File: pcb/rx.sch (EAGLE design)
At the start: 34 parts, among them Y1 CRYSTAL-26MHZSMD-3.2X2.5

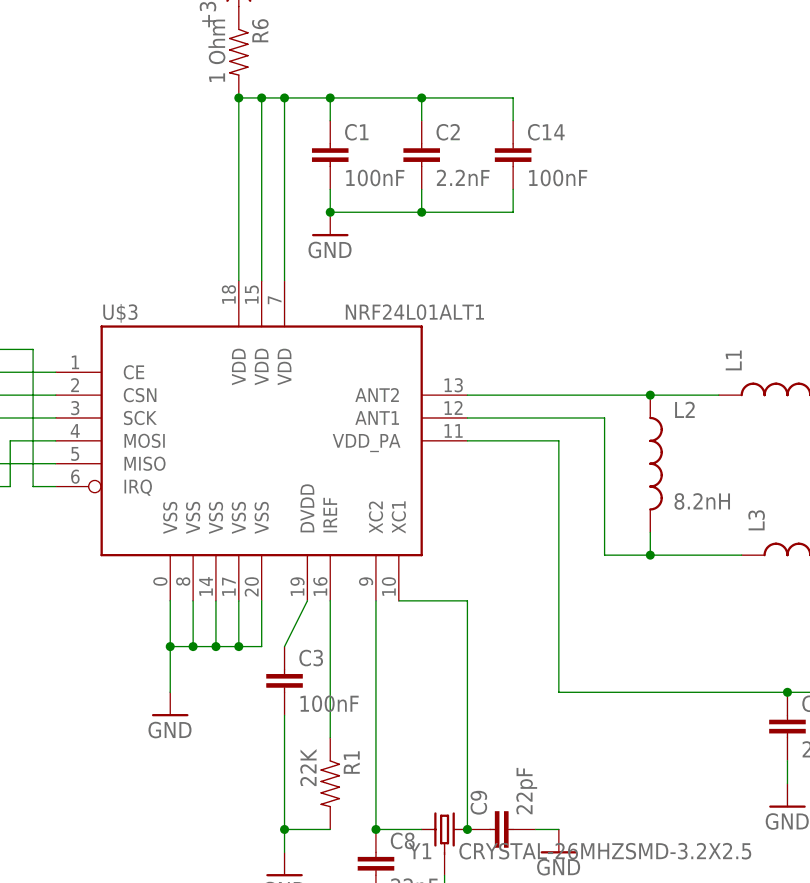
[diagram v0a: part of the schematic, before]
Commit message: adjusted RF section
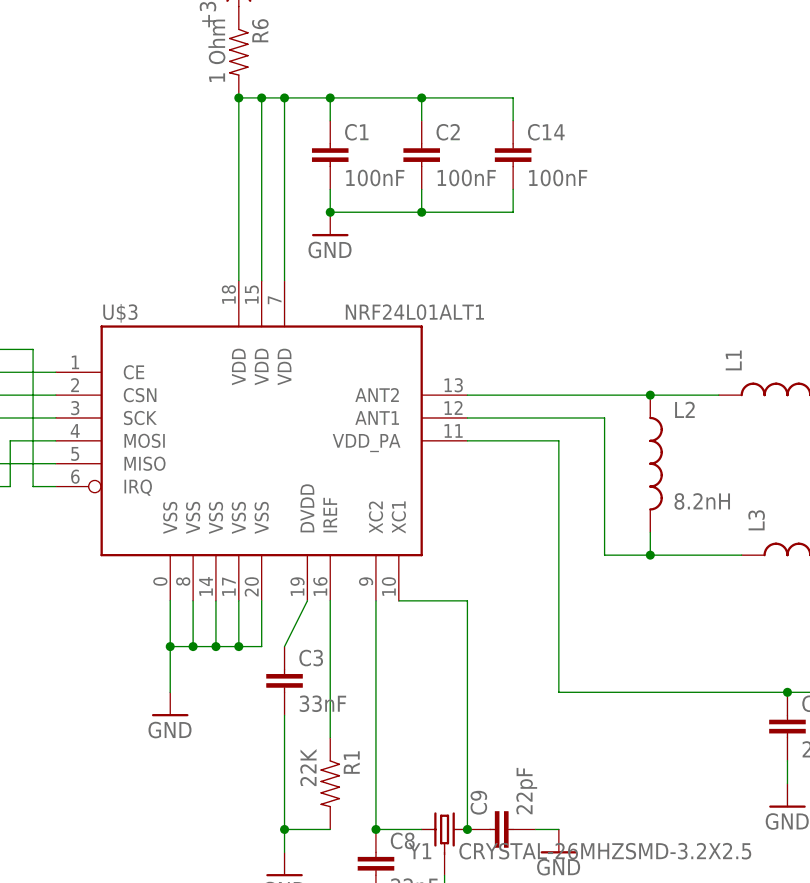
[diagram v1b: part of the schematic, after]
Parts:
- C2: value 2.2nF -> 100nF
- C3: value 100nF -> 33nF
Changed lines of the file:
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@@
 <part name="GND12" library="clock" deviceset="GND" device=""/>
 <part name="R1" library="joyAnalog" deviceset="RESISTOR" device="0805-RES" value="22K"/>
-<part name="C2" library="clock" deviceset="CAP" device="0805" value="2.2nF"/>
-<part name="C3" library="clock" deviceset="CAP" device="0805" value="100nF"/>
+<part name="C2" library="clock" deviceset="CAP" device="0805" value="100nF"/>
+<part name="C3" library="clock" deviceset="CAP" device="0805" value="33nF"/>
 <part name="GND2" library="clock" deviceset="GND" device=""/>
 <part name="L1" library="basicBoard" deviceset="INDUCTOR" device="0805" value="3.9nH"/>

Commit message: rev3 working
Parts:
- C1, C14, C2: value 100nF -> 4.7uF
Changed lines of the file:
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@@
 <part name="+3V1" library="supply1" library_urn="urn:adsk.eagle:library:371" deviceset="+3V3" device=""/>
 <part name="GND1" library="supply1" library_urn="urn:adsk.eagle:library:371" deviceset="GND" device=""/>
-<part name="C1" library="clock" deviceset="CAP" device="0805" value="100nF"/>
+<part name="C1" library="clock" deviceset="CAP" device="0805" value="4.7uF"/>
 <part name="GND12" library="clock" deviceset="GND" device=""/>
 <part name="R1" library="joyAnalog" deviceset="RESISTOR" device="0805-RES" value="22K"/>
-<part name="C2" library="clock" deviceset="CAP" device="0805" value="100nF"/>
+<part name="C2" library="clock" deviceset="CAP" device="0805" value="4.7uF"/>
 <part name="C3" library="clock" deviceset="CAP" device="0805" value="33nF"/>
 <part name="GND2" library="clock" deviceset="GND" device=""/>
@@
 <part name="GND13" library="supply1" library_urn="urn:adsk.eagle:library:371" deviceset="GND" device=""/>
 <part name="R6" library="joyAnalog" deviceset="RESISTOR" device="0805-RES" value="1 Ohm"/>
-<part name="C14" library="clock" deviceset="CAP" device="0805" value="100nF"/>
+<part name="C14" library="clock" deviceset="CAP" device="0805" value="4.7uF"/>
 </parts>
 <sheets>

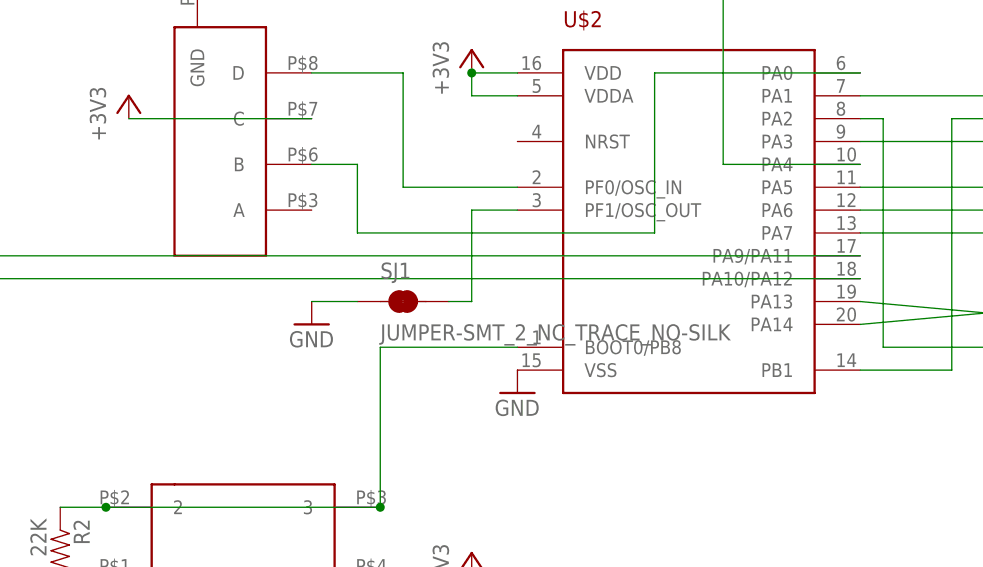
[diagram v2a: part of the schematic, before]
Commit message: tx board removed jumper
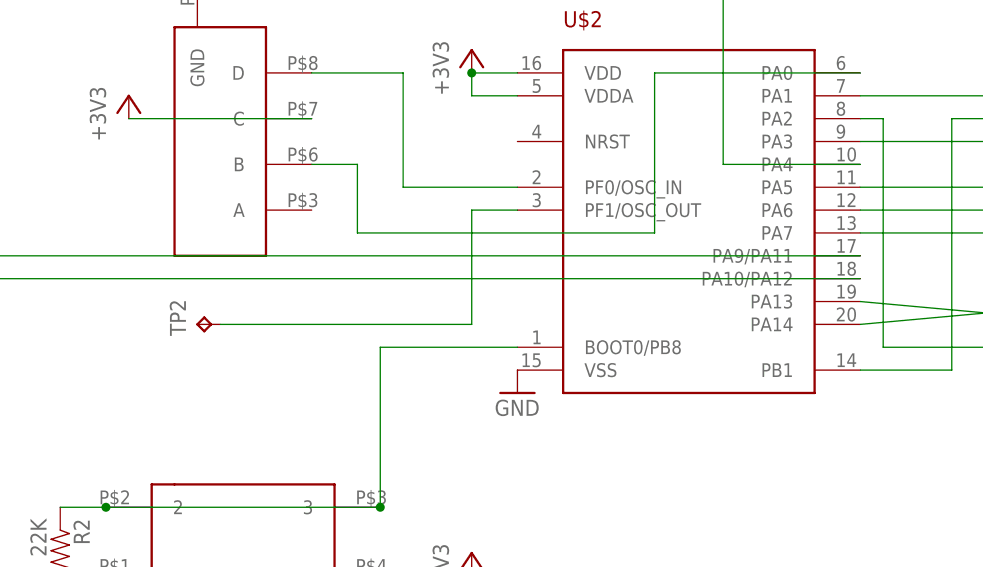
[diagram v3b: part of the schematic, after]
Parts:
- removed SJ1: JUMPER-SMT_2_NC_TRACE_NO-SILK, SparkFun-Jumpers:JUMPER-SMT_2_NC_TRACE_NO-SILK
- added TP2: TPTP12R, testpad:TPTP12R
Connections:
- net GND: no longer SJ1.1
- net N$19: now also TP2.TP; no longer SJ1.2
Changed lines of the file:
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@@
 <part name="R4" library="joyAnalog" deviceset="RESISTOR" device="0805-RES" value="5.1K"/>
 <part name="P+1" library="supply1" library_urn="urn:adsk.eagle:library:371" deviceset="+5V" device=""/>
-<part name="SJ1" library="SparkFun-Jumpers" deviceset="JUMPER-SMT_2_NC_TRACE" device="_NO-SILK"/>
 <part name="U$10" library="3pos_slide_switch" deviceset="324_SW" device="324_SWITCH_FOOT_HOLE" value="324_SW324_SWITCH_FOOT_HOLE"/>
 <part name="LED2" library="joyAnalog" deviceset="LED" device="CHIP-LED0805"/>
@@
 <part name="E1" library="SparkFun-RF" deviceset="ANTENNA-GROUNDED" device="TRACE-15.2MM"/>
 <part name="GND6" library="clock" deviceset="GND" device=""/>
-<part name="GND13" library="supply1" library_urn="urn:adsk.eagle:library:371" deviceset="GND" device=""/>
 <part name="R6" library="joyAnalog" deviceset="RESISTOR" device="0805-RES" value="1 Ohm"/>
 <part name="C14" library="clock" deviceset="CAP" device="0805" value="4.7uF"/>
+<part name="TP2" library="testpad" library_urn="urn:adsk.eagle:library:385" deviceset="TP" device="TP12R" package3d_urn="urn:adsk.eagle:package:27963/1"/>
 </parts>
 <sheets>
@@
 <instance part="R4" gate="G$1" x="30.48" y="43.18"/>
 <instance part="P+1" gate="1" x="-137.16" y="0"/>
-<instance part="SJ1" gate="G$1" x="0" y="0"/>
 <instance part="U$10" gate="G$1" x="-17.78" y="-27.94"/>
 <instance part="LED2" gate="G$1" x="17.78" y="43.18" rot="R270"/>
@@
 <instance part="E1" gate="G$1" x="241.3" y="17.78" rot="R270"/>
 <instance part="GND6" gate="1" x="231.14" y="7.62"/>
-<instance part="GND13" gate="1" x="-10.16" y="-2.54"/>
 <instance part="R6" gate="G$1" x="116.84" y="55.88" rot="R270"/>
 <instance part="C14" gate="G$1" x="147.32" y="43.18"/>
+<instance part="TP2" gate="G$1" x="-22.86" y="-2.54" rot="R90"/>
 </instances>
 <busses>
@@
 <pinref part="GND6" gate="1" pin="GND"/>
 <wire x1="231.14" y1="15.24" x2="231.14" y2="10.16" width="0.1524" layer="91"/>
-</segment>
-<segment>
-<pinref part="SJ1" gate="G$1" pin="1"/>
-<wire x1="-10.16" y1="0" x2="-5.08" y2="0" width="0.1524" layer="91"/>
-<pinref part="GND13" gate="1" pin="GND"/>
 </segment>
 </net>
@@
 <pinref part="U$2" gate="G$1" pin="PF1/OSC_OUT"/>
 <wire x1="12.7" y1="10.16" x2="7.62" y2="10.16" width="0.1524" layer="91"/>
-<wire x1="7.62" y1="10.16" x2="7.62" y2="0" width="0.1524" layer="91"/>
-<pinref part="SJ1" gate="G$1" pin="2"/>
-<wire x1="7.62" y1="0" x2="5.08" y2="0" width="0.1524" layer="91"/>
+<wire x1="7.62" y1="10.16" x2="7.62" y2="-2.54" width="0.1524" layer="91"/>
+<wire x1="7.62" y1="-2.54" x2="-20.32" y2="-2.54" width="0.1524" layer="91"/>
+<pinref part="TP2" gate="G$1" pin="TP"/>
 </segment>
 </net>
@@
 will not be understood (or retained) with this version.
 </note>
+<note version="8.3" severity="warning">
+Since Version 8.3, EAGLE supports the association of 3D packages
+with devices in libraries, schematics, and board files. Those 3D
+packages will not be understood (or retained) with this version.
+</note>
 </compatibility>

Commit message: before trail run
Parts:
- C3: value 33nF -> 100nF
- C8, C9: value 22pF -> 12pF
- Y1: value CRYSTAL-26MHZSMD-3.2X2.5 -> 16MHz_12pF
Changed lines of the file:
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@@
 <part name="R1" library="joyAnalog" deviceset="RESISTOR" device="0805-RES" value="22K"/>
 <part name="C2" library="clock" deviceset="CAP" device="0805" value="4.7uF"/>
-<part name="C3" library="clock" deviceset="CAP" device="0805" value="33nF"/>
+<part name="C3" library="clock" deviceset="CAP" device="0805" value="100nF"/>
 <part name="GND2" library="clock" deviceset="GND" device=""/>
 <part name="L1" library="basicBoard" deviceset="INDUCTOR" device="0805" value="3.9nH"/>
@@
 <part name="GND5" library="clock" deviceset="GND" device=""/>
 <part name="GND8" library="clock" deviceset="GND" device=""/>
-<part name="C8" library="clock" deviceset="CAP" device="0805" value="22pF"/>
+<part name="C8" library="clock" deviceset="CAP" device="0805" value="12pF"/>
 <part name="GND10" library="clock" deviceset="GND" device=""/>
-<part name="C9" library="clock" deviceset="CAP" device="0805" value="22pF"/>
+<part name="C9" library="clock" deviceset="CAP" device="0805" value="12pF"/>
 <part name="GND11" library="clock" deviceset="GND" device=""/>
 <part name="U$4" library="3pos_slide_switch" deviceset="XC6206_DEV" device=""/>
@@
 <part name="GND16" library="supply1" library_urn="urn:adsk.eagle:library:371" deviceset="GND" device=""/>
 <part name="GND17" library="supply1" library_urn="urn:adsk.eagle:library:371" deviceset="GND" device=""/>
-<part name="Y1" library="SparkFun-Clocks" deviceset="CRYSTAL-26MHZ" device="SMD-3.2X2.5"/>
+<part name="Y1" library="SparkFun-Clocks" deviceset="CRYSTAL-26MHZ" device="SMD-3.2X2.5" value="16MHz_12pF"/>
 <part name="R2" library="joyAnalog" deviceset="RESISTOR" device="0805-RES" value="22K"/>
 <part name="GND9" library="supply1" library_urn="urn:adsk.eagle:library:371" deviceset="GND" device=""/>
@@
 <instance part="GND10" gate="1" x="132.08" y="-45.72"/>
 <instance part="C9" gate="G$1" x="147.32" y="-30.48" rot="R90"/>
-<instance part="GND11" gate="1" x="152.4" y="-33.02"/>
+<instance part="GND11" gate="1" x="162.56" y="-33.02"/>
 <instance part="U$4" gate="G$1" x="-116.84" y="-7.62"/>
 <instance part="C10" gate="G$1" x="-137.16" y="-10.16"/>
@@
 <pinref part="C9" gate="G$1" pin="2"/>
 <pinref part="GND11" gate="1" pin="GND"/>
-<wire x1="152.4" y1="-30.48" x2="149.86" y2="-30.48" width="0.1524" layer="91"/>
+<wire x1="162.56" y1="-30.48" x2="149.86" y2="-30.48" width="0.1524" layer="91"/>
 </segment>
 <segment>

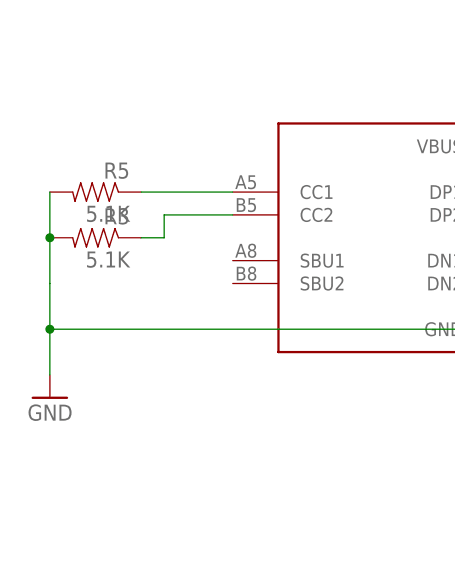
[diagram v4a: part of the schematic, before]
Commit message: centered usbc footprint, adjusted board layout
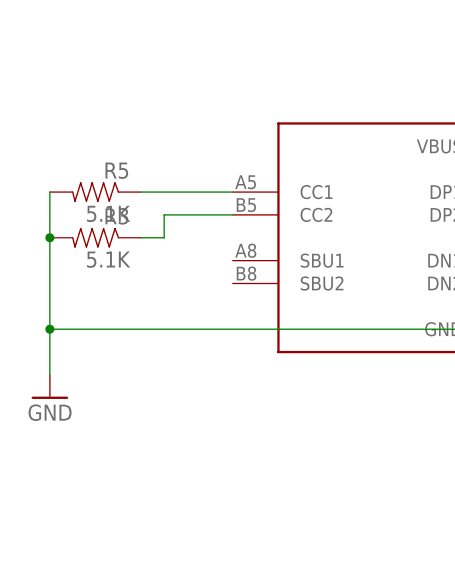
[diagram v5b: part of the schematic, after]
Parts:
- removed U$6: USBC_16P, my_usbc_16p:USBC_16P
- added U$7: USBC_16P_CENTERED, my_usbc_16p_centered:USBC_16P_CENTERED
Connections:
- net +5V: now also U$7.VBUS; no longer U$6.VBUS
- net GND: now also U$7.GND; no longer U$6.GND
- net N$12: now also U$7.DN1, U$7.DN2; no longer U$6.DN1, U$6.DN2
- net N$13: now also U$7.DP1, U$7.DP2; no longer U$6.DP1, U$6.DP2
- net N$25: now also U$7.CC2; no longer U$6.CC2
- net N$27: now also U$7.CC1; no longer U$6.CC1
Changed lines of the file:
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@@
 <part name="U$5" library="adafruit_changed" deviceset="PINHD5" device=""/>
 <part name="+3V5" library="supply1" library_urn="urn:adsk.eagle:library:371" deviceset="+3V3" device=""/>
-<part name="U$6" library="my_usbc_16p" deviceset="USBC_16P" device=""/>
 <part name="GND21" library="supply1" deviceset="GND" device=""/>
 <part name="R3" library="joyAnalog" deviceset="RESISTOR" device="0805-RES" value="5.1K"/>
@@
 <part name="C14" library="clock" deviceset="CAP" device="0805" value="4.7uF"/>
 <part name="TP2" library="testpad" library_urn="urn:adsk.eagle:library:385" deviceset="TP" device="TP12R" package3d_urn="urn:adsk.eagle:package:27963/1"/>
+<part name="U$7" library="my_usbc_16p_centered" deviceset="USBC_16P_CENTERED" device=""/>
 </parts>
 <sheets>
@@
 <instance part="U$5" gate="G$1" x="81.28" y="-7.62"/>
 <instance part="+3V5" gate="G$1" x="-30.48" y="22.86"/>
-<instance part="U$6" gate="G$1" x="-172.72" y="-22.86" rot="MR0"/>
 <instance part="GND21" gate="1" x="-210.82" y="-30.48" rot="MR0"/>
 <instance part="R3" gate="G$1" x="-205.74" y="-12.7" rot="MR0"/>
@@
 <instance part="C14" gate="G$1" x="147.32" y="43.18"/>
 <instance part="TP2" gate="G$1" x="-22.86" y="-2.54" rot="R90"/>
+<instance part="U$7" gate="G$1" x="-172.72" y="-22.86" rot="MR0"/>
 </instances>
 <busses>
@@
 <segment>
 <pinref part="GND21" gate="1" pin="GND"/>
-<wire x1="-210.82" y1="-17.78" x2="-210.82" y2="-22.86" width="0.1524" layer="91"/>
 <pinref part="R3" gate="G$1" pin="2"/>
 <wire x1="-210.82" y1="-22.86" x2="-210.82" y2="-27.94" width="0.1524" layer="91"/>
-<wire x1="-210.82" y1="-12.7" x2="-210.82" y2="-17.78" width="0.1524" layer="91"/>
+<wire x1="-210.82" y1="-12.7" x2="-210.82" y2="-22.86" width="0.1524" layer="91"/>
 <junction x="-210.82" y="-12.7"/>
 <pinref part="R5" gate="G$1" pin="2"/>
 <wire x1="-210.82" y1="-7.62" x2="-210.82" y2="-12.7" width="0.1524" layer="91"/>
-<pinref part="U$6" gate="G$1" pin="GND"/>
 <wire x1="-157.48" y1="-22.86" x2="-210.82" y2="-22.86" width="0.1524" layer="91"/>
 <junction x="-210.82" y="-22.86"/>
+<pinref part="U$7" gate="G$1" pin="GND"/>
 </segment>
 <segment>
@@
 <wire x1="-144.78" y1="-7.62" x2="-152.4" y2="-7.62" width="0.1524" layer="91"/>
 <wire x1="-152.4" y1="-7.62" x2="-152.4" y2="-15.24" width="0.1524" layer="91"/>
-<pinref part="U$6" gate="G$1" pin="DN1"/>
-<pinref part="U$6" gate="G$1" pin="DN2"/>
 <wire x1="-157.48" y1="-15.24" x2="-157.48" y2="-17.78" width="0.1524" layer="91"/>
 <wire x1="-152.4" y1="-15.24" x2="-157.48" y2="-15.24" width="0.1524" layer="91"/>
+<pinref part="U$7" gate="G$1" pin="DN1"/>
 <junction x="-157.48" y="-15.24"/>
+<pinref part="U$7" gate="G$1" pin="DN2"/>
 </segment>
 </net>
@@
 <pinref part="U$2" gate="G$1" pin="PA10/PA12"/>
 <wire x1="50.8" y1="2.54" x2="-142.24" y2="2.54" width="0.1524" layer="91"/>
-<pinref part="U$6" gate="G$1" pin="DP1"/>
-<pinref part="U$6" gate="G$1" pin="DP2"/>
 <wire x1="-157.48" y1="-7.62" x2="-157.48" y2="-10.16" width="0.1524" layer="91"/>
 <wire x1="-142.24" y1="-10.16" x2="-157.48" y2="-10.16" width="0.1524" layer="91"/>
+<pinref part="U$7" gate="G$1" pin="DP1"/>
+<pinref part="U$7" gate="G$1" pin="DP2"/>
 <junction x="-157.48" y="-10.16"/>
 </segment>
@@
 <pinref part="P+1" gate="1" pin="+5V"/>
 <wire x1="-137.16" y1="-2.54" x2="-137.16" y2="-5.08" width="0.1524" layer="91"/>
-<pinref part="U$6" gate="G$1" pin="VBUS"/>
 <wire x1="-137.16" y1="-5.08" x2="-157.48" y2="-5.08" width="0.1524" layer="91"/>
 <wire x1="-157.48" y1="-5.08" x2="-157.48" y2="-2.54" width="0.1524" layer="91"/>
+<pinref part="U$7" gate="G$1" pin="VBUS"/>
 </segment>
 </net>
@@
 <wire x1="-190.5" y1="-10.16" x2="-198.12" y2="-10.16" width="0.1524" layer="91"/>
 <wire x1="-198.12" y1="-10.16" x2="-198.12" y2="-12.7" width="0.1524" layer="91"/>
-<pinref part="U$6" gate="G$1" pin="CC2"/>
+<pinref part="U$7" gate="G$1" pin="CC2"/>
 </segment>
 </net>
@@
 <pinref part="R5" gate="G$1" pin="1"/>
 <wire x1="-190.5" y1="-7.62" x2="-200.66" y2="-7.62" width="0.1524" layer="91"/>
-<pinref part="U$6" gate="G$1" pin="CC1"/>
-</segment>
-</net>
+<pinref part="U$7" gate="G$1" pin="CC1"/>
+</segment>
+</net>

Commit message: foodprint adjustment, coord file
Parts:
- removed U$1: SW_3POS_DEVSW_3POS_OFFICIAL, 3pos_slide_switch:SW_3POS_DEVSW_3POS_OFFICIAL
- added SW1: SW_3POS_DEVSW_3POS_OFFICIAL, 3pos_slide_switch_centered:SW_3POS_DEVSW_3POS_OFFICIAL
- renumbered U$10 to SW2, U$2 to IC1, U$3 to IC2, U$4 to U2, U$7 to U1
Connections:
- net +3V3: now also SW1.C; no longer U$1.C
- net GND: now also SW1.GND; no longer U$1.GND
- net N$10: now also SW1.D; no longer U$1.D
- net N$26: now also SW1.B; no longer U$1.B

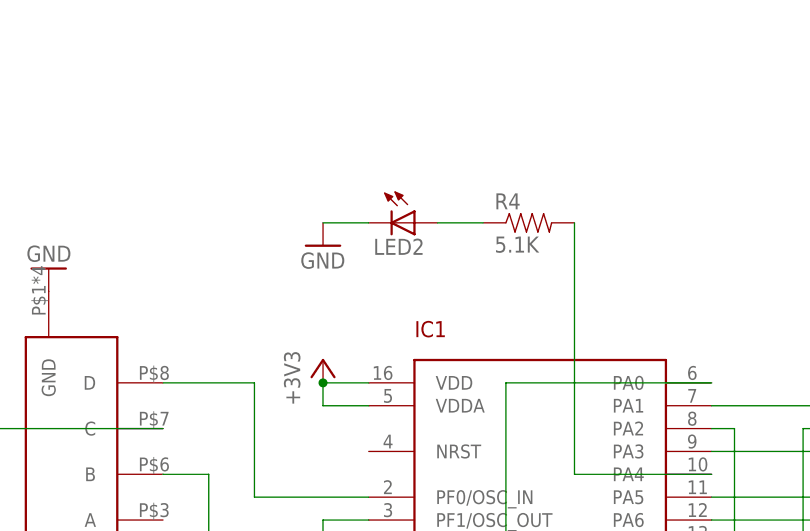
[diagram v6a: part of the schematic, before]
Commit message: adjusted timing budget, distance under 15mm are now ignored
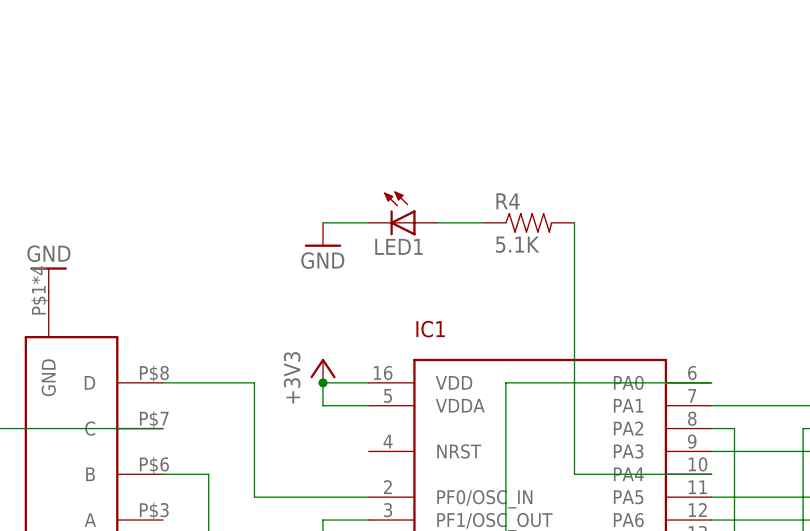
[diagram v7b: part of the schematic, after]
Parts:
- renumbered LED2 to LED1
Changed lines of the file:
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@@
 <part name="P+1" library="supply1" library_urn="urn:adsk.eagle:library:371" deviceset="+5V" device=""/>
 <part name="SW2" library="3pos_slide_switch" deviceset="324_SW" device="324_SWITCH_FOOT_HOLE" value="324_SW324_SWITCH_FOOT_HOLE"/>
-<part name="LED2" library="joyAnalog" deviceset="LED" device="CHIP-LED0805"/>
+<part name="LED1" library="joyAnalog" deviceset="LED" device="CHIP-LED0805"/>
 <part name="GND22" library="supply1" library_urn="urn:adsk.eagle:library:371" deviceset="GND" device=""/>
 <part name="IC1" library="tx" deviceset="STM32F042F4" device=""/>
@@
 <instance part="P+1" gate="1" x="-137.16" y="0"/>
 <instance part="SW2" gate="G$1" x="-17.78" y="-27.94"/>
-<instance part="LED2" gate="G$1" x="17.78" y="43.18" rot="R270"/>
+<instance part="LED1" gate="G$1" x="17.78" y="43.18" rot="R270"/>
 <instance part="GND22" gate="1" x="7.62" y="40.64"/>
 <instance part="IC1" gate="G$1" x="30.48" y="10.16"/>
@@
 <segment>
 <pinref part="GND22" gate="1" pin="GND"/>
-<pinref part="LED2" gate="G$1" pin="C"/>
+<pinref part="LED1" gate="G$1" pin="C"/>
 <wire x1="7.62" y1="43.18" x2="12.7" y2="43.18" width="0.1524" layer="91"/>
 </segment>
@@
 <pinref part="R4" gate="G$1" pin="1"/>
 <wire x1="20.32" y1="43.18" x2="25.4" y2="43.18" width="0.1524" layer="91"/>
-<pinref part="LED2" gate="G$1" pin="A"/>
-</segment>
-</net>
+<pinref part="LED1" gate="G$1" pin="A"/>
+</segment>
+</net>
